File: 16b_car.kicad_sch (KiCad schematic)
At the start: 8 parts, among them M1 Motor_DC, M2 Motor_DC, Q1 Q_NPN_BCE, SW1 SW_DIP_x01

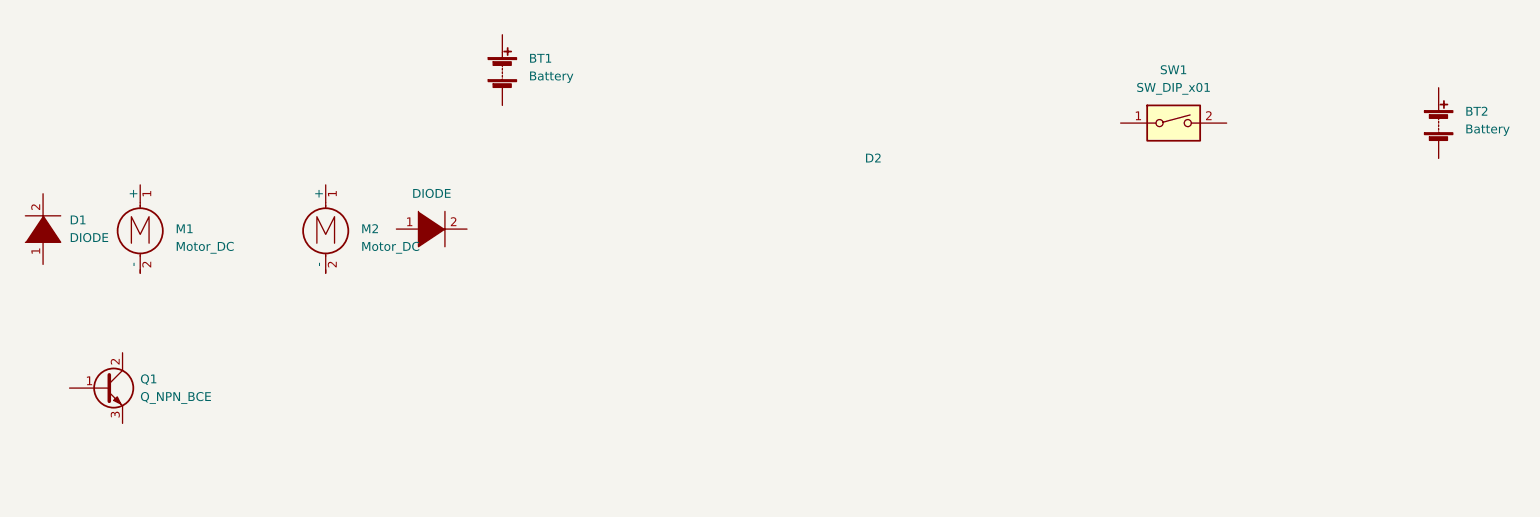
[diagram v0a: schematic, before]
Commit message: motor circuit complete
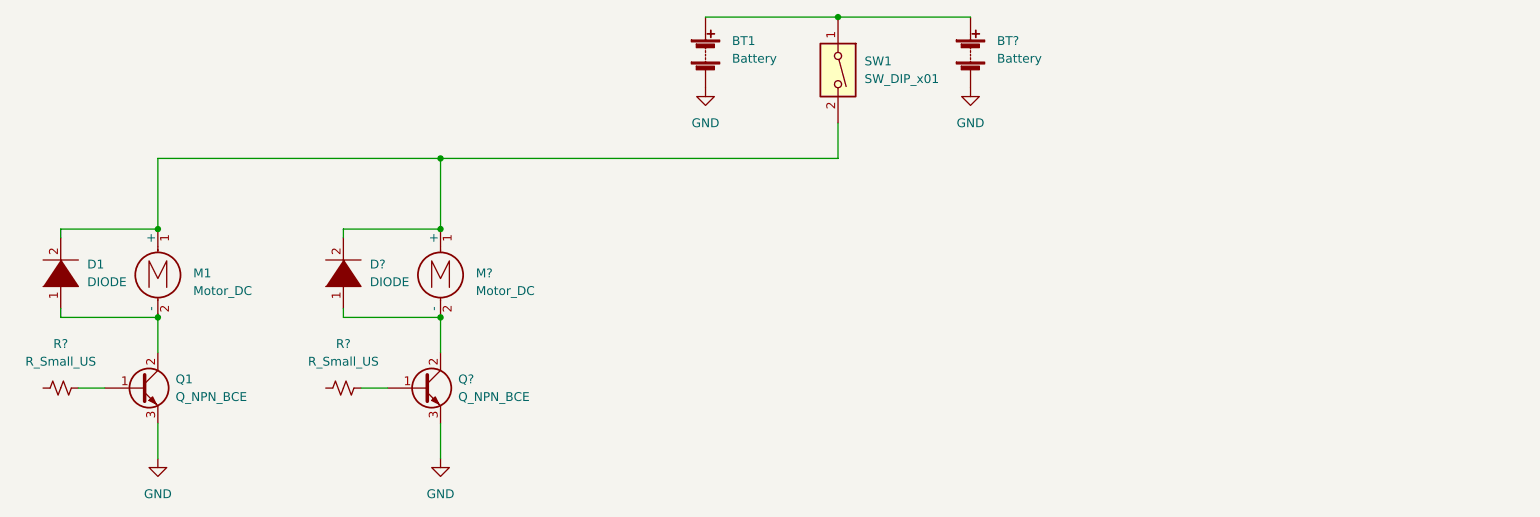
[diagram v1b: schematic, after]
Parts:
- removed BT2: Battery, symbol Device:Battery
- removed D2: DIODE, symbol pspice:DIODE
- removed M2: Motor_DC, symbol Motor:Motor_DC
- added BT?: Battery, symbol Device:Battery
- added D?: DIODE, symbol pspice:DIODE
- added M?: Motor_DC, symbol Motor:Motor_DC
- added Q?: Q_NPN_BCE, Package_TO_SOT_SMD:SOT-89-3_Handsoldering, symbol Device:Q_NPN_BCE
- added R? (x2): R_Small_US, symbol Device:R_Small_US
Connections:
- net at D1.1 (K): now also M1.2 (-), Q1.2 (C)
- net at D1.2 (A): now also M1.1 (+), SW1.2, D?.2 (A), M?.1 (+)
- net at SW1.1: now also BT1.1 (+), BT?.1 (+)
- net GND: now reaches BT1.2 (-)
- net GND: now also Q1.3 (E), BT?.2 (-), Q?.3 (E)
- net at Q1.1 (B): now also R?.2
- new net: Q?.1 (B), R?.2
- new net: D?.1 (K), M?.2 (-), Q?.2 (C)
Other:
- moved on the sheet: BT1, D1, M1, Q1, SW1

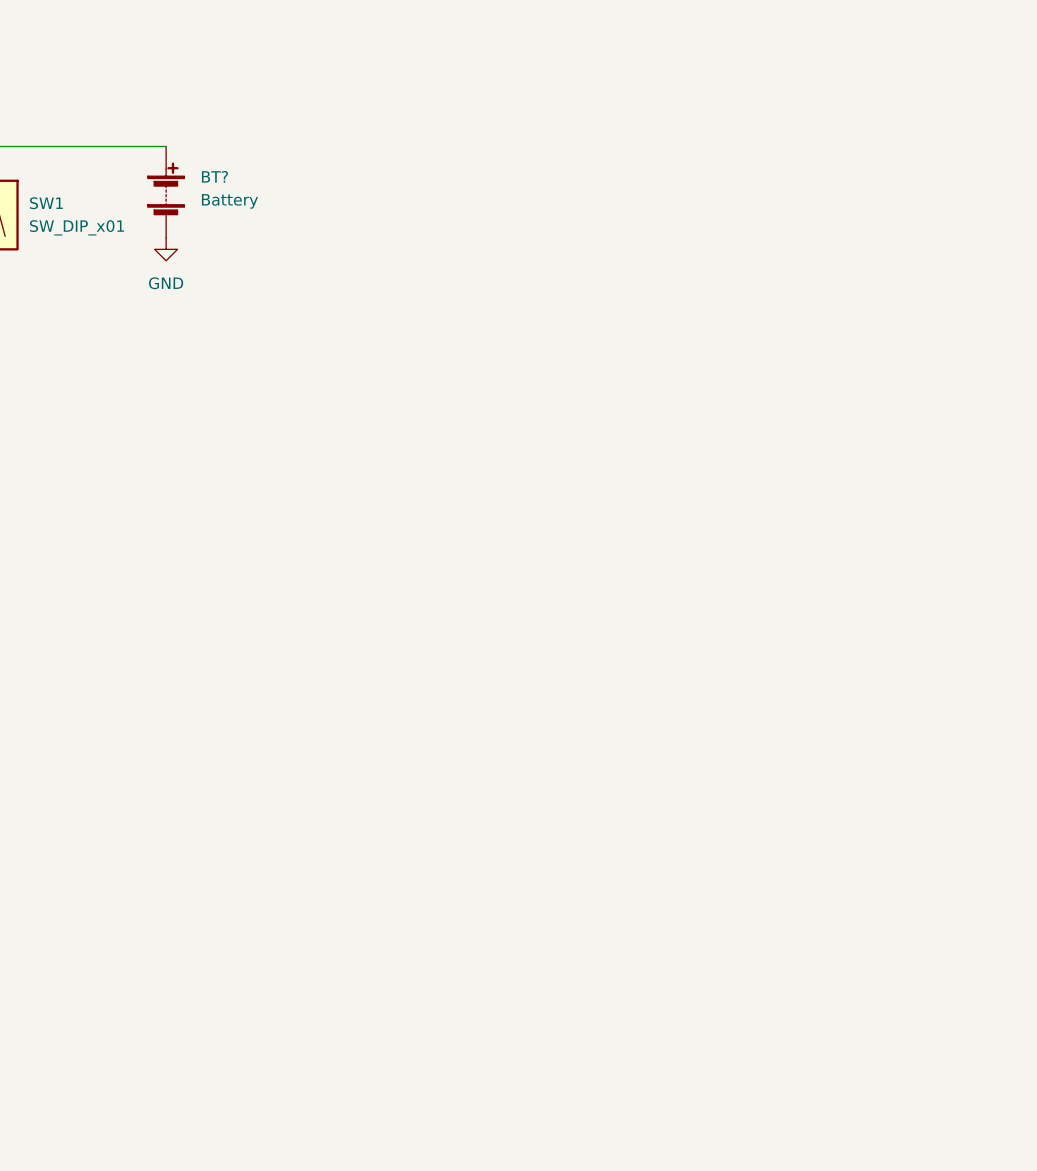
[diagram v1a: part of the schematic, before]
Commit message: regulator circuits added to schematic
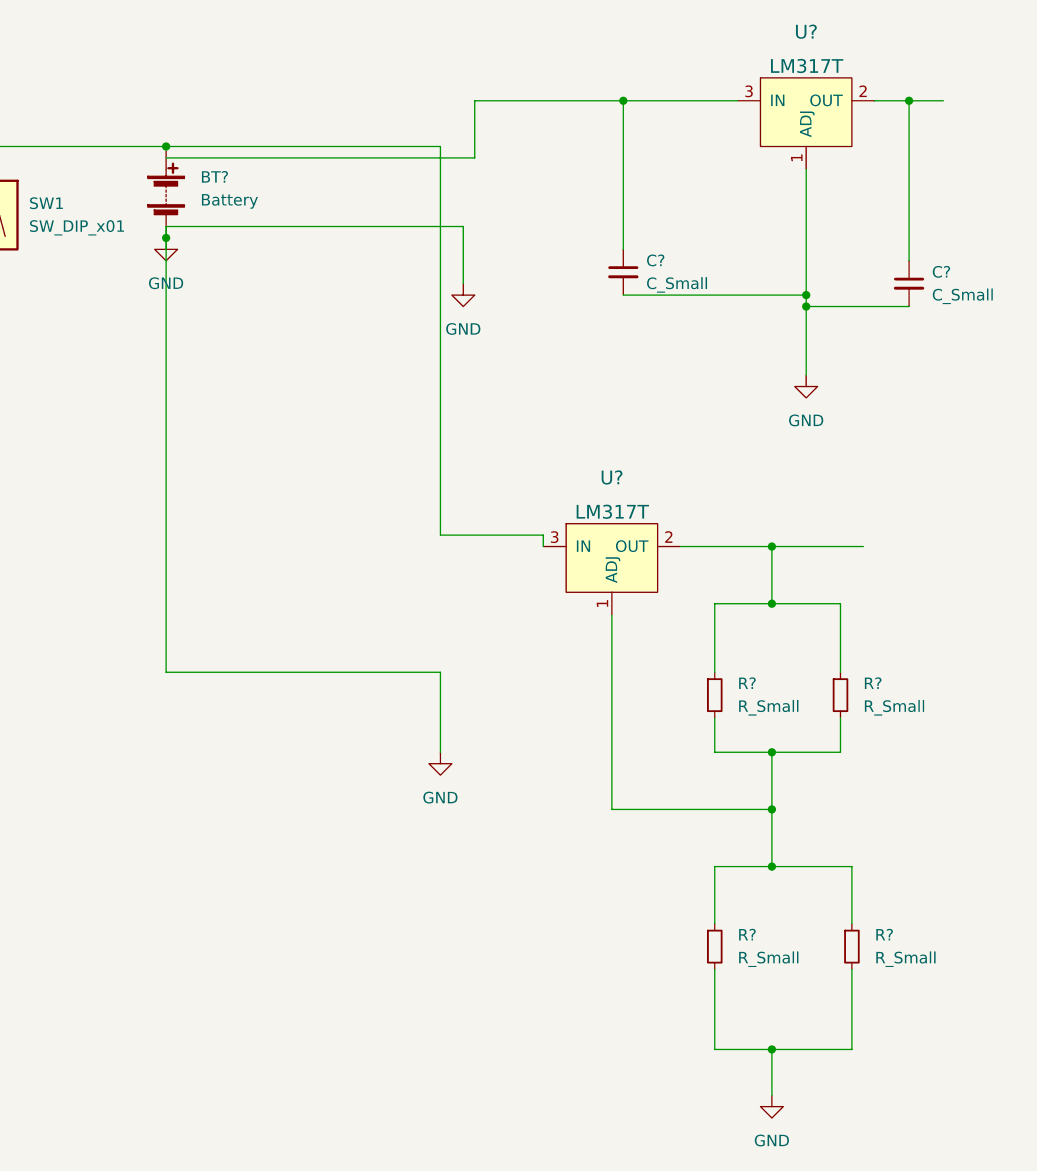
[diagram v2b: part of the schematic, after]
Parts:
- added C? (x2): C_Small, symbol Device:C_Small
- added R? (x4): R_Small, symbol Device:R_Small
- added U? (x2): LM317T, digikey-footprints:TO-220-3, symbol dk_PMIC-Voltage-Regulators-Linear:LM317T
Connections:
- net GND: now also C?.2, C?.2, R?.2, R?.2, U?.1 (ADJ)
- net at BT1.1 (+), BT?.1 (+), SW1.1: now also U?.3 (IN)
- new net: C?.1, U?.2 (OUT)
- new net: C?.1, U?.3 (IN)
- new net: R?.1, R?.1, U?.2 (OUT)
- new net: R?.1, R?.1, R?.2, R?.2, U?.1 (ADJ)

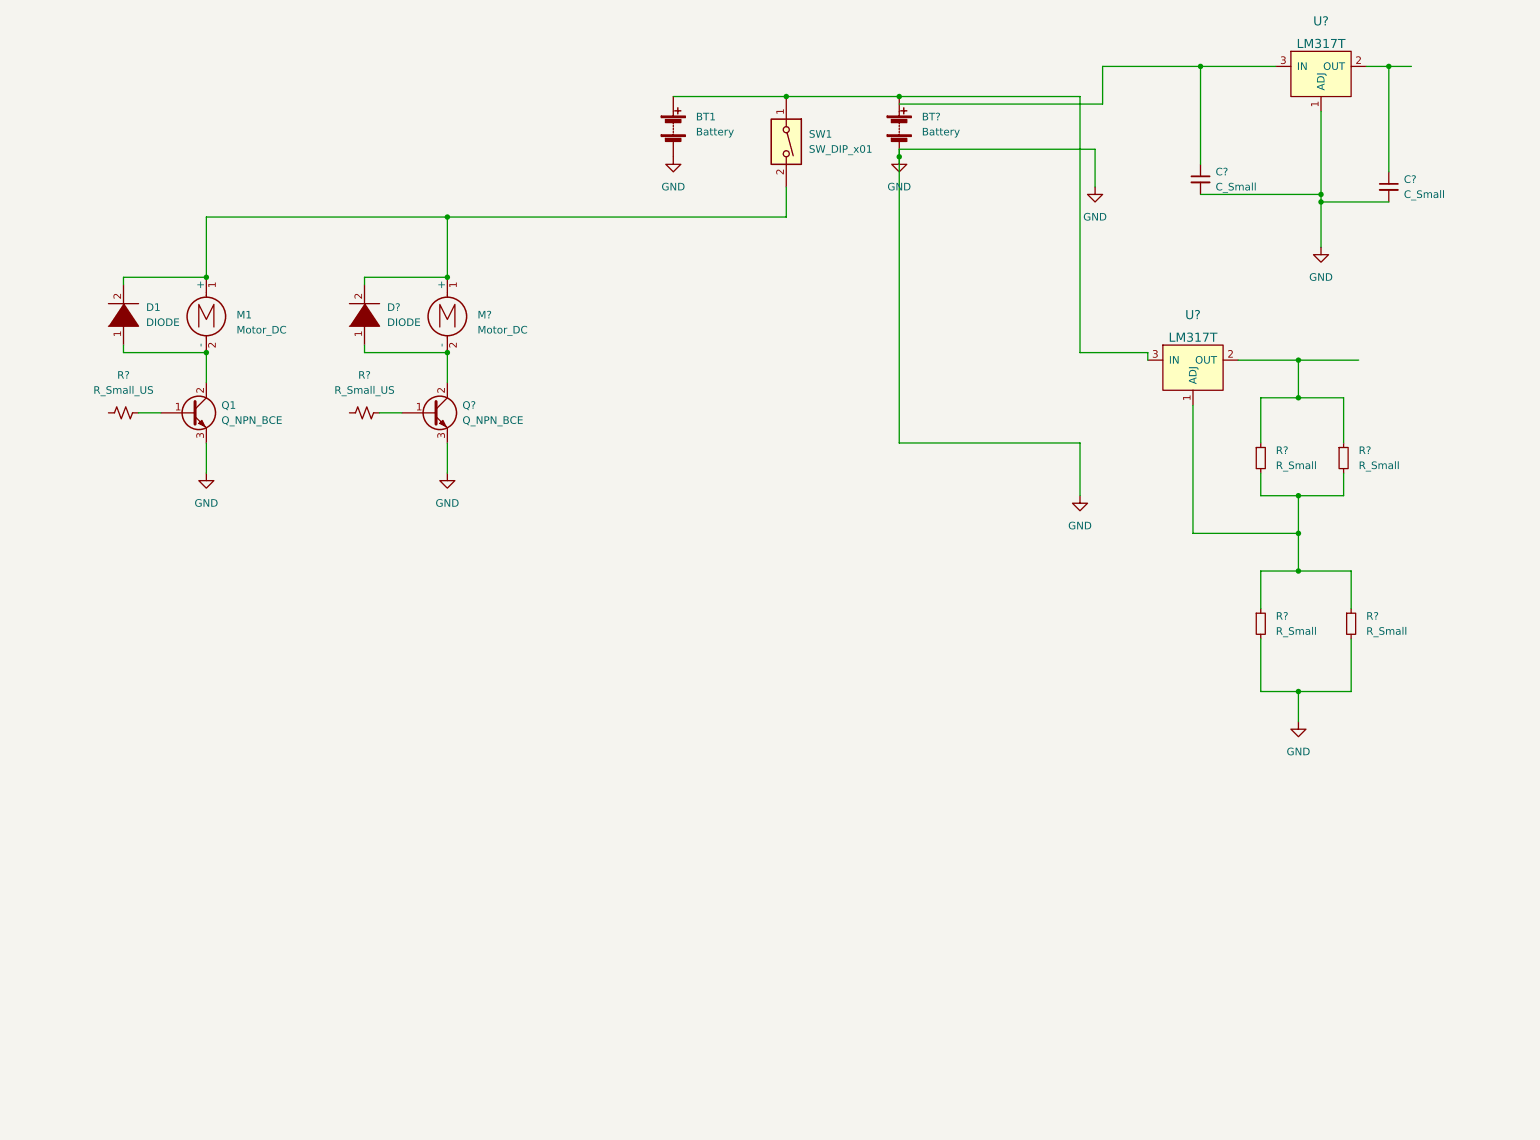
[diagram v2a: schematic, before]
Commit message: finished the schematic for everything. added annotations and component values. TODO: check ERC with TAs
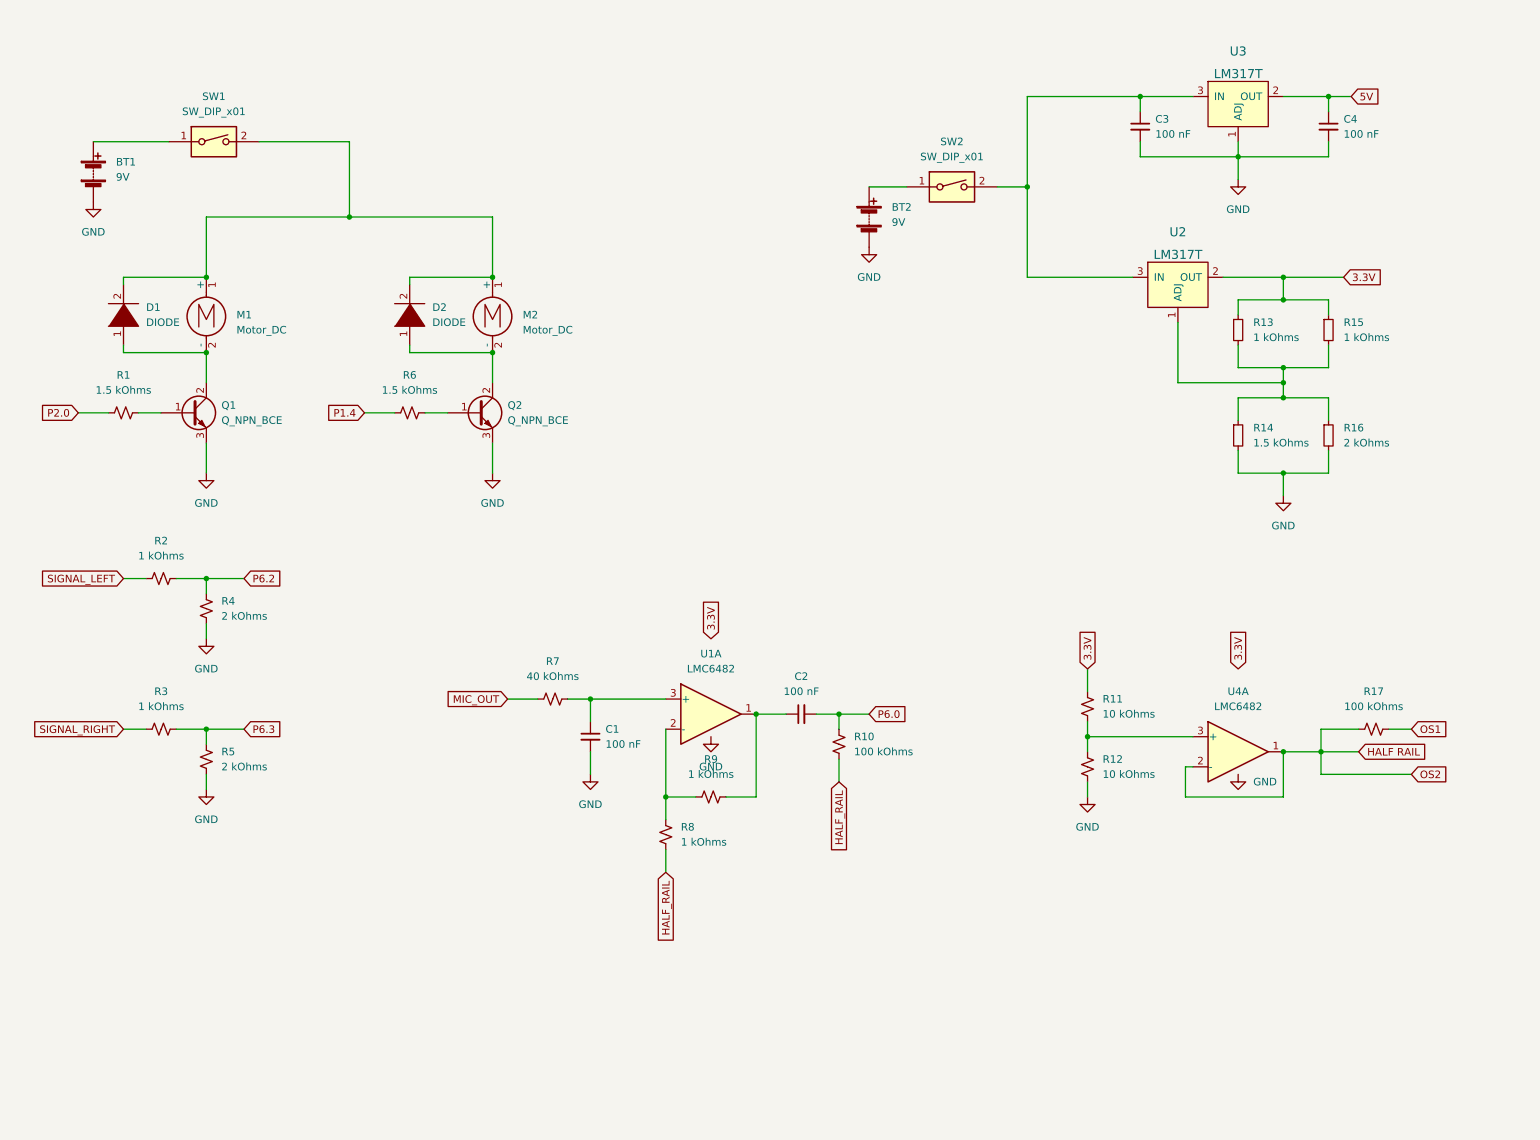
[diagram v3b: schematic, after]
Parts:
- added C1, C2: 100 nF, symbol Device:C_Small
- added R10, R17: 100 kOhms, symbol Device:R_Small_US
- added R11, R12: 10 kOhms, symbol Device:R_Small_US
- added R2, R3, R8, R9: 1 kOhms, symbol Device:R_Small_US
- added R4, R5: 2 kOhms, symbol Device:R_Small_US
- added R7: 40 kOhms, symbol Device:R_Small_US
- added SW2: SW_DIP_x01, symbol Switch:SW_DIP_x01
- added U1, U4: LMC6482, symbol Amplifier_Operational:LMC6482
- BT1: value Battery -> 9V
- BT2: renamed from BT?; value Battery -> 9V
- C3, C4: renamed from C?; value C_Small -> 100 nF
- R1, R6: renamed from R?; value R_Small_US -> 1.5 kOhms
- R13, R15: renamed from R?; value R_Small -> 1 kOhms
- R14: renamed from R?; value R_Small -> 1.5 kOhms
- R16: renamed from R?; value R_Small -> 2 kOhms
- gave numbers to parts that had none: 5
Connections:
- net GND: now also C1.2, R12.1, R4.1, R5.1
- net at BT1.1 (+), SW1.1: no longer BT2.1 (+), U2.3 (IN)
- net P2.0: now reaches R1.1
- net P1.4: now reaches R6.1
- net 5V: now reaches C4.1, U3.2 (OUT)
- net at C3.1, U3.3 (IN): now also U2.3 (IN), SW2.2
- net 3.3V: now reaches R13.1, R15.1, U2.2 (OUT)
- net 3.3V: now also R11.2
- new net: R11.1, R12.2, U4.3 (+)
- new net: BT2.1 (+), SW2.1
- new net: C2.1, R9.1, U1.1
- new net: C1.1, R7.1, U1.3 (+)
- new net: R8.1, R9.2, U1.2 (-)
- new net HALF RAIL: R17.2, U4.1, U4.2 (-)
- new net HALF_RAIL: R10.2, R8.2
- new net MIC_OUT: R7.2
- new net OS1: R17.1
- new net P6.0: C2.2, R10.1
- new net P6.2: R2.2, R4.2
- new net P6.3: R3.2, R5.2
- new net SIGNAL_LEFT: R2.1
- new net SIGNAL_RIGHT: R3.1
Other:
- moved on the sheet: BT1, BT2, C3, C4, D2, M2, Q2, R13, R14, R15, R16, R6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

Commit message: footprints added
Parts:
- removed C2: 100 nF, symbol Device:C_Small
- removed R10, R17: 100 kOhms, symbol Device:R_Small_US
- removed R8, R9: 1 kOhms, symbol Device:R_Small_US
- removed U1, U4: LMC6482, symbol Amplifier_Operational:LMC6482
- added C?: 100 nF, symbol Device:C_Small
- added R? (x2): 100 kOhms, Resistor_SMD:R_0805_2012Metric_Pad1.20x1.40mm_HandSolder, symbol Device:R_Small_US
- added R? (x2): 1 kOhms, Resistor_SMD:R_0805_2012Metric_Pad1.20x1.40mm_HandSolder, symbol Device:R_Small_US
- added U?: LM6482IN/NOPB, sixteen_b_car:lm6482_pdip, symbol sixteen_symbols:LM6482IN/NOPB
- C3, C4: footprint (none) -> Capacitor_SMD:C_0805_2012Metric_Pad1.18x1.45mm_HandSolder
- D1, D2: footprint (none) -> Diode_SMD:D_SMA_Handsoldering
- R1, R11, R12, R13, R14, R15, R16, R2, R3, R4, R5, R6, R7: footprint (none) -> Resistor_SMD:R_0805_2012Metric_Pad1.20x1.40mm_HandSolder
- SW1: footprint (none) -> sixteen_b_car:slide_switch
- SW2: footprint (none) -> sixteen_b_car:SW_DPDT_CK_JS202011JCQN
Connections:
- net 3.3V: now also U2.3 (OUT); no longer U2.2 (OUT)
- net GND: now also U3.2 (ADJ), U?.4; no longer U3.1 (ADJ)
- net HALF RAIL: now also R?.2, U?.1, U?.2
- net HALF_RAIL: now also R?.2, R?.2
- net OS1: now also R?.1
- net P6.0: now also C?.2, R?.1
- net at R11.1, R12.2: now also U?.3
- net at C3.1, SW2.2: now also U2.1 (IN), U3.1 (IN); no longer U2.3 (IN), U3.3 (IN)
- net at R13.2, R14.1, R15.2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: now also U2.2 (ADJ); no longer U2.1 (ADJ)
- net at C1.1, R7.1: now also U?.5
- new net: R?.1, R?.2, U?.6
- new net: C?.1, R?.1, U?.7
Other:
- moved on the sheet: C1, R11, R12, R7
